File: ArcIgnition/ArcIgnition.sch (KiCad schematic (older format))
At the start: 7 parts

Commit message: Fixing the mistakes as always
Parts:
- added T?: Transformer_1P_1S, symbol Device:Transformer_1P_1S
- J?: value Screw_Terminal_01x02 -> Electrodes
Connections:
- net labels removed: TransPin2
- wire segments 18 -> 28
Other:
- moved on the sheet: C?, D?, J?, K?, Q?

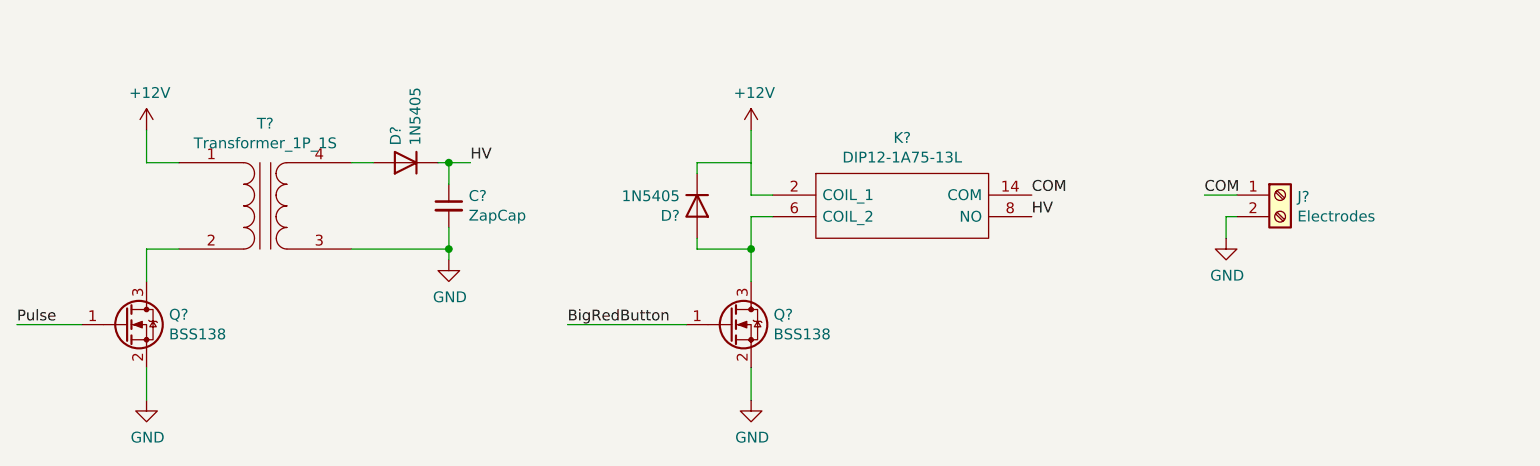
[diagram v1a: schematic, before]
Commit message: Ungrounded the secondary circuit
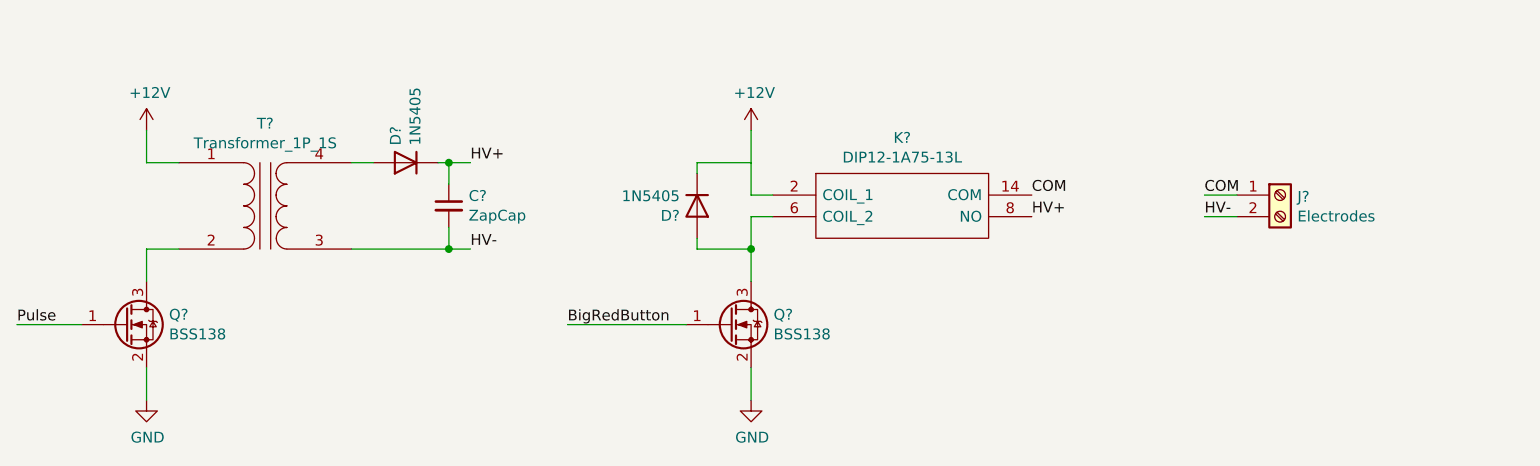
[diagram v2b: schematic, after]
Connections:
- net GND: no longer C?.2, J?.2 (Pin_2), T?.3 (SA)
- net HV renamed HV+
- new net HV-: C?.2, J?.2 (Pin_2), T?.3 (SA)
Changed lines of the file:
@@
-$EndComp
-$Comp
-L power:GND #PWR?
-U 1 1 5FB466FD
-P 3850 2750
-F 0 "#PWR?" H 3850 2500 50  0001 C CNN
-F 1 "GND" H 3855 2577 50  0000 C CNN
-F 2 "" H 3850 2750 50  0001 C CNN
-F 3 "" H 3850 2750 50  0001 C CNN
-	1    3850 2750
-	1    0    0    -1
-$EndComp
-Wire Wire Line
-	7500 2550 7450 2550
-Wire Wire Line
-	7450 2550 7450 2650
-$Comp
-L power:GND #PWR?
-U 1 1 5FB48C9E
-P 7450 2650
-F 0 "#PWR?" H 7450 2400 50  0001 C CNN
-F 1 "GND" H 7455 2477 50  0000 C CNN
-F 2 "" H 7450 2650 50  0001 C CNN
-F 3 "" H 7450 2650 50  0001 C CNN
-	1    7450 2650
-	1    0    0    -1
 $EndComp
 $Comp
@@
 COM
 Text Label 6550 2550 0    50   ~ 0
-HV
+HV+
 Text Label 4400 3050 0    50   ~ 0
 BigRedButton
@@
 Connection ~ 3850 2300
 Text Label 3950 2300 0    50   ~ 0
-HV
+HV+
 Wire Wire Line
 	3850 2600 3850 2700
@@
 Wire Wire Line
 	3400 2700 3850 2700
-Connection ~ 3850 2700
-Wire Wire Line
-	3850 2700 3850 2750
 Wire Wire Line
 	5000 2700 5000 2650
@@
 Wire Wire Line
 	4400 3050 4950 3050
+Wire Wire Line
+	3850 2700 3950 2700
+Connection ~ 3850 2700
+Text Label 3950 2700 0    50   ~ 0
+HV-
+Wire Wire Line
+	7500 2550 7350 2550
+Text Label 7350 2550 0    50   ~ 0
+HV-
 $EndSCHEMATC
